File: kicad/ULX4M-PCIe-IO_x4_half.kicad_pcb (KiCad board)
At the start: 4 copper layers, 167.7 x 111.2 mm, 53 parts, among them J1 PCIexpress_bracket, J10 FCR684205R, J11 OLED, J12 641737-1, J13 39-30-0060, J2 PCIexpress_x4, J3 SFP+, J4 SFP+, J5 Conn_02x20_Odd_Even, J6 Conn_02x05_Odd_Even, J7 Micro_SD_Card_CD, J8 Conn_02x05_Odd_Even, J9 FCR684205T, P1 HDMI-D, SW1 SW_DIP_x08, SW2 SW_DIP_x08, U1 TPD4E02B04DQA, U10 TPD4E02B04DQA, U11 TPD4E02B04DQA, U12 TPD4E02B04DQA, U13 AT24CS32-SSHM, U2 TPD4E02B04DQA, U3 TPD4E02B04DQA, U4 TPD4E02B04DQA, U5 TPD4E02B04DQA, U6 TPD4E02B04DQA, U7 TPD4E02B04DQA, U8 TPD4E02B04DQA, U9 TPD4E02B04DQA

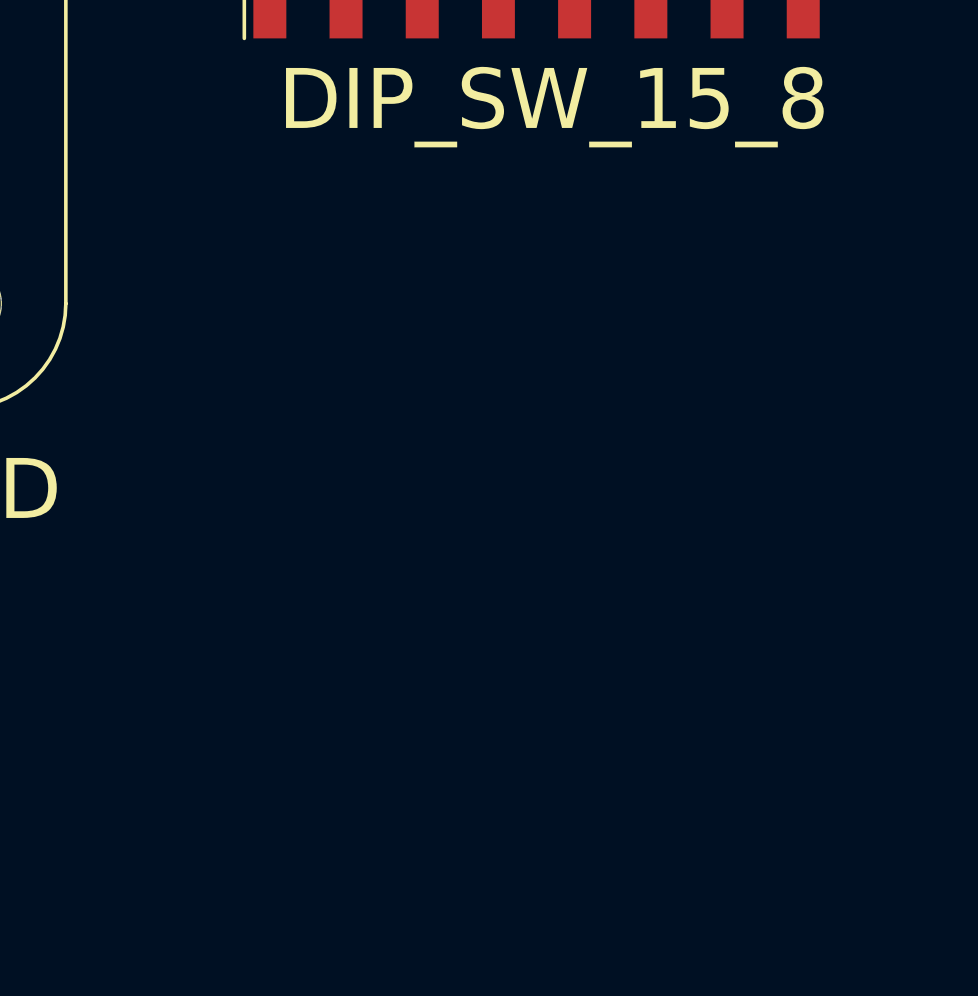
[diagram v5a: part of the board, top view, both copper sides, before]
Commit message: Adding LEDs fix #4
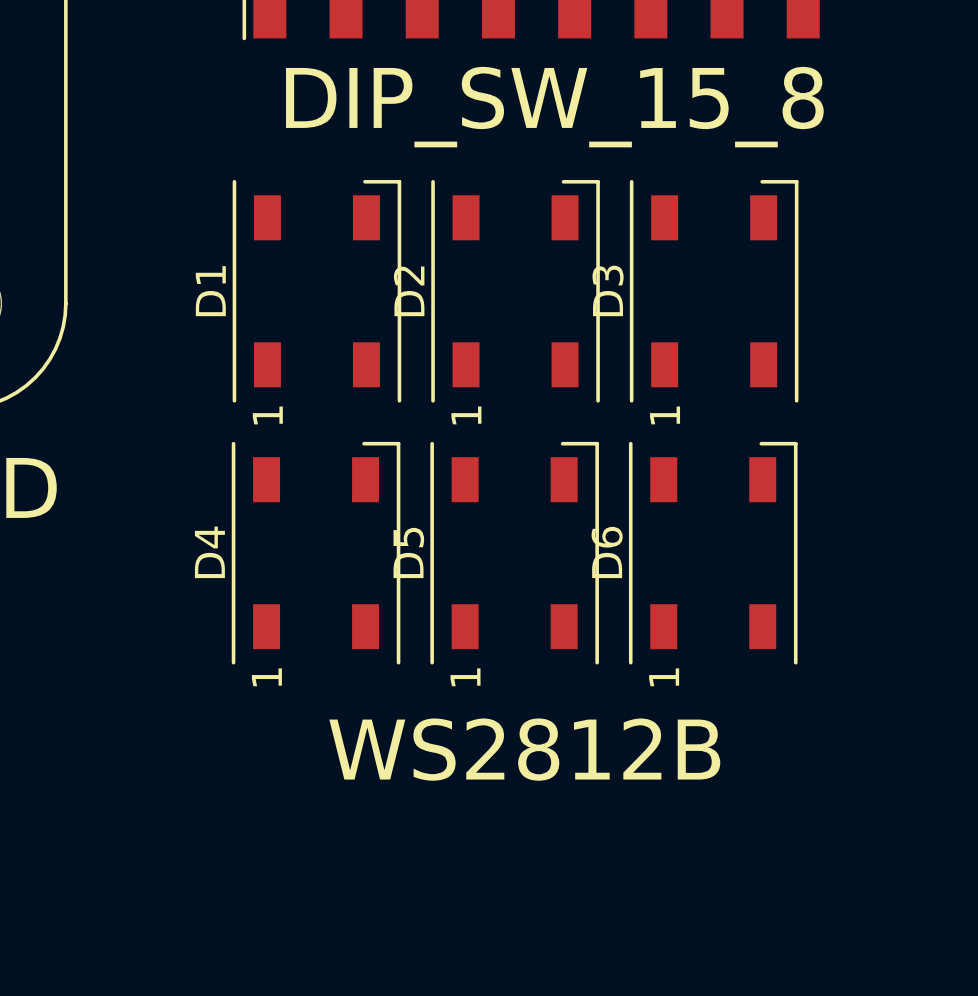
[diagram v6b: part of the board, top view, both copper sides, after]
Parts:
- added D1: WS2812B, LED_SMD:LED_WS2812B_PLCC4_5.0x5.0mm_P3.2mm, F.Cu at (172.9, 120.0)
- added D2: WS2812B, LED_SMD:LED_WS2812B_PLCC4_5.0x5.0mm_P3.2mm, F.Cu at (179.5, 120.0)
- added D3: WS2812B, LED_SMD:LED_WS2812B_PLCC4_5.0x5.0mm_P3.2mm, F.Cu at (186.1, 120.0)
- added D4: WS2812B, LED_SMD:LED_WS2812B_PLCC4_5.0x5.0mm_P3.2mm, F.Cu at (172.9, 128.7)
- added D5: WS2812B, LED_SMD:LED_WS2812B_PLCC4_5.0x5.0mm_P3.2mm, F.Cu at (179.5, 128.7)
- added D6: WS2812B, LED_SMD:LED_WS2812B_PLCC4_5.0x5.0mm_P3.2mm, F.Cu at (186.1, 128.7)
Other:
- board text added: "WS2812B"

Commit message: Adding more features
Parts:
- added C10: 100nF, Capacitor_SMD:C_0603_1608Metric, F.Cu at (205.0, 113.7)
- added C11: 10nF, Capacitor_SMD:C_0603_1608Metric, F.Cu at (205.0, 115.2)
- added C9: 330nF, Capacitor_SMD:C_0603_1608Metric, F.Cu at (213.3, 103.6)
- added D10: +3.3VA, LED_SMD:LED_0603_1608Metric, F.Cu at (161.8, 160.8)
- added D7: +12V, LED_SMD:LED_0603_1608Metric, F.Cu at (161.7, 152.2)
- added D8: +5V, LED_SMD:LED_0603_1608Metric, F.Cu at (161.7, 155.1)
- added D9: +3.3V, LED_SMD:LED_0603_1608Metric, F.Cu at (161.8, 157.9)
- added F1: Fuse_5V, Fuse:Fuse_1206_3216Metric, F.Cu at (204.4, 101.0)
- added F2: Fuse_12V, Fuse:Fuse_1206_3216Metric, F.Cu at (222.1, 101.0)
- added H1: HATMountingHole, MountingHole:MountingHole_3.2mm_M3, F.Cu at (173.4, 115.6)
- added H2: HATMountingHole, MountingHole:MountingHole_3.2mm_M3, F.Cu at (222.4, 115.6)
- added H3: HATMountingHole, MountingHole:MountingHole_3.2mm_M3, F.Cu at (173.4, 173.6)
- added H4: HATMountingHole, MountingHole:MountingHole_3.2mm_M3, F.Cu at (222.4, 173.6)
- added H5: OLEDMountingHole, MountingHole:MountingHole_3.2mm_M3, F.Cu at (120.2, 142.8)
- added H6: OLEDMountingHole, MountingHole:MountingHole_3.2mm_M3, F.Cu at (120.2, 172.9)
- added H7: OLEDMountingHole, MountingHole:MountingHole_3.2mm_M3, F.Cu at (149.5, 142.8)
- added H8: OLEDMountingHole, MountingHole:MountingHole_3.2mm_M3, F.Cu at (149.5, 173.2)
- added J14: LM7805_EN, Connector_PinHeader_2.54mm:PinHeader_1x02_P2.54mm_Vertical, F.Cu at (204.5, 106.5)
- added J15: POE, Connector_PinHeader_2.54mm:PinHeader_2x02_P2.54mm_Vertical, F.Cu at (217.5, 172.3)
- added R10: R220, Resistor_SMD:R_0603_1608Metric, F.Cu at (164.9, 155.1)
- added R11: R120, Resistor_SMD:R_0603_1608Metric, F.Cu at (164.9, 157.9)
- added R12: R120, Resistor_SMD:R_0603_1608Metric, F.Cu at (165.0, 160.8)
- added R9: R510, Resistor_SMD:R_0603_1608Metric, F.Cu at (164.9, 152.2)
- added U14: LM78M05_TO252, Package_TO_SOT_SMD:TO-252-2, F.Cu at (210.2, 110.3)
- AE1: value Antenna_Dipole -> EXT_CLK_REF1; footprint Connector_Coaxial:SMA_Amphenol_132289_EdgeMount -> Connector_Coaxial:SMA_Amphenol_132291-12_Vertical
- AE2: value Antenna_Dipole -> EXT_CLK_REF2; footprint Connector_Coaxial:SMA_Amphenol_132289_EdgeMount -> Connector_Coaxial:SMA_Amphenol_132291-12_Vertical
- J5: value Conn_02x20_Odd_Even -> HAT; footprint Connector_PinHeader_2.54mm:PinHeader_2x20_P2.54mm_Vertical_SMD -> Connector_PinHeader_2.54mm:PinHeader_2x20_P2.54mm_Vertical
- J6: value Conn_02x05_Odd_Even -> EXT_USB; footprint Connector_PinHeader_2.54mm:PinHeader_2x05_P2.54mm_Vertical_SMD -> Connector_PinHeader_2.54mm:PinHeader_2x05_P2.54mm_Vertical
- J7: footprint micro-sd:SCHD3A100 -> Connector_Card:microSD_HC_Molex_104031-0811
- J8: value Conn_02x05_Odd_Even -> Board_To_Board
- P1: footprint hdmi-d:HDMI-D -> conn-fci:CONN-10029449-111RLF
- moved AE1 263.6 mm to (88.8, 110.1)
- moved AE2 252.9 mm to (88.9, 121.1)
- moved G*** 129.0 mm to (78.0, 92.9)
- moved radiona 129.0 mm to (74.2, 88.3)
- moved REF** 102.1 mm to (101.9, 113.8)
- moved REF** 86.3 mm to (102.1, 134.4)
- moved J7 79.0 mm to (172.8, 92.1)
- moved SW2 60.0 mm to (125.4, 130.7)
- moved J5 53.9 mm to (221.1, 120.5), turned to 0 degrees
- moved SW1 50.6 mm to (148.6, 130.7)
- moved J11 39.3 mm to (119.7, 167.9), turned to 180 degrees
- moved J13 38.5 mm to (187.2, 97.8), turned to 180 degrees
- moved U13 22.8 mm to (184.2, 174.5)
- moved D1 10.9 mm to (165.6, 128.1), turned to 180 degrees
- moved D2 10.1 mm to (173.6, 128.1), turned to 180 degrees
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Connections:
- J12 pad 1: +12V -> Net-(J12-Pad1)
- J12 pad 4: +5V -> Net-(J12-Pad4)
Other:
- board text added: "5V/12V"
- board text added: "EXT_REF_CLK1"
- board text added: "EXT_REF_CLK2"
- board text added: "PCIe 12V"
- board text added: "PoE"
- board text added: "Raspberry Pi HaT compatible"
- board text removed: "GPIO"
- board text removed: "Power IN"
